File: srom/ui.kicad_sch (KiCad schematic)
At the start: 8 parts

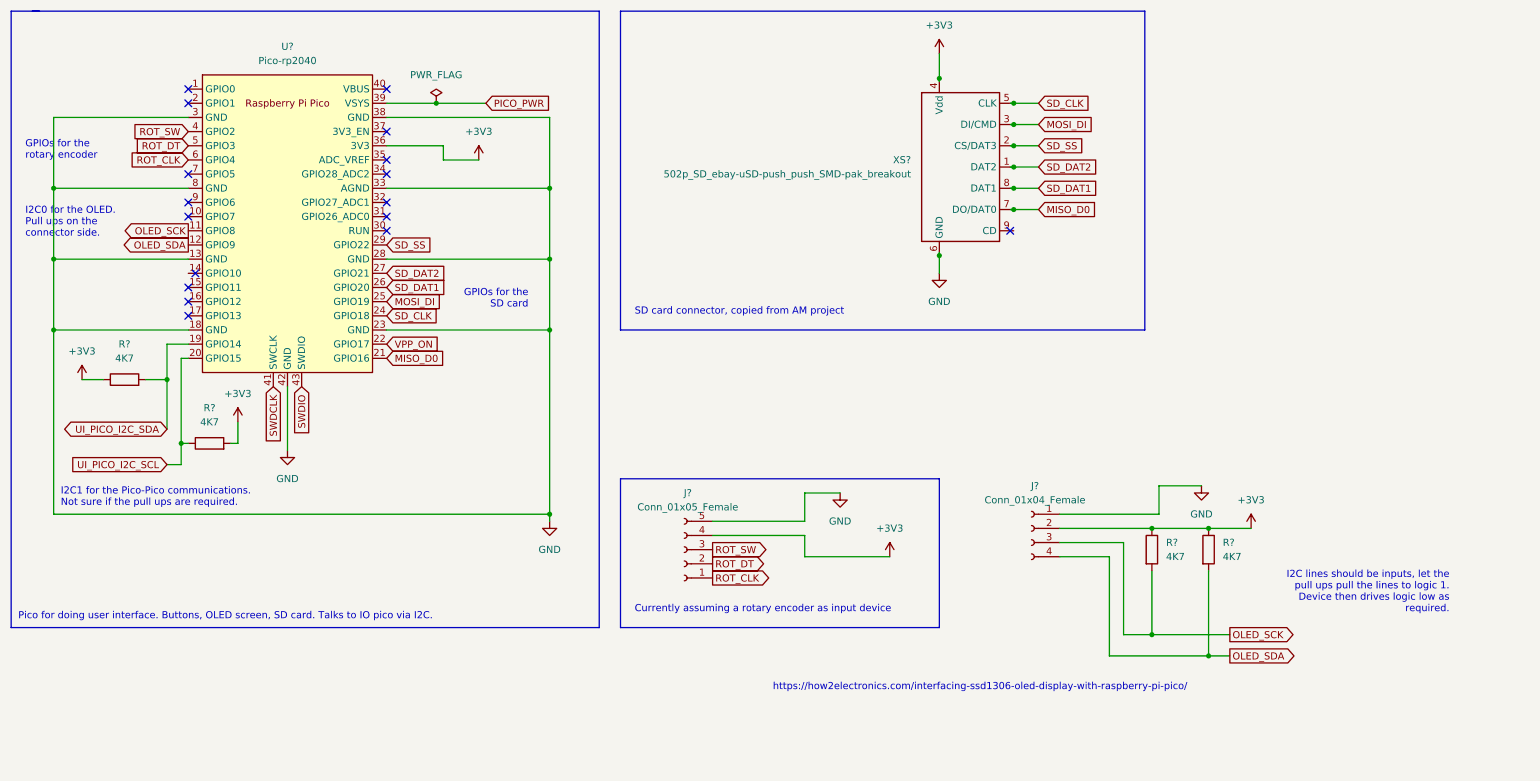
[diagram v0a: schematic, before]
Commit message: schematics complete for IO and UI picos
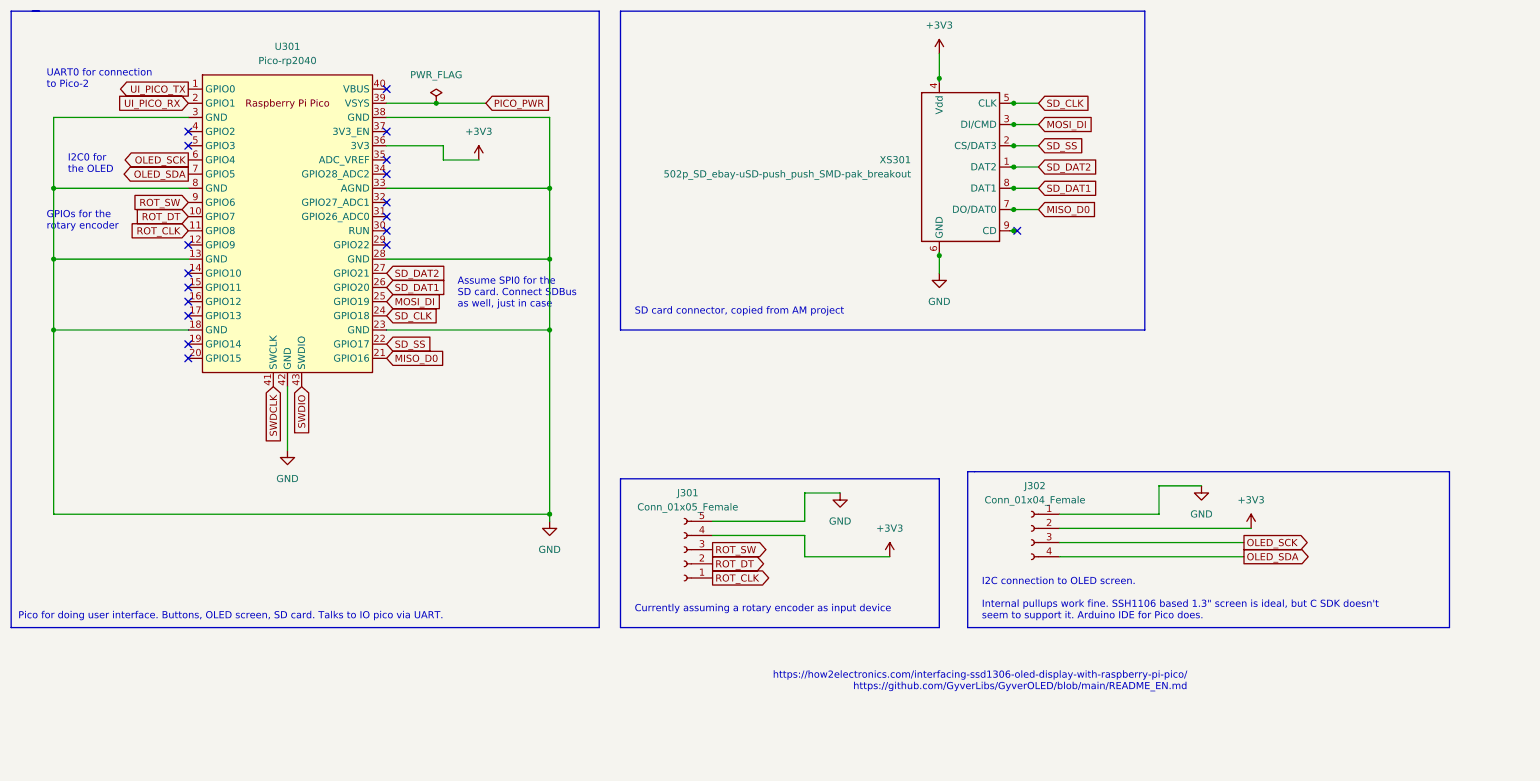
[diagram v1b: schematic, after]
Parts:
- removed R? (x4): 4K7, symbol Device:R
- gave numbers to parts that had none: 4
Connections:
- net VPP_ON is gone; now on net SD_SS: U301.22 (GPIO17)
- net OLED_SCK: now also U301.6 (GPIO4); no longer U301.11 (GPIO8)
- net OLED_SDA: now also U301.7 (GPIO5); no longer U301.12 (GPIO9)
- net ROT_CLK: now also U301.11 (GPIO8); no longer U301.6 (GPIO4)
- net ROT_DT: now also U301.10 (GPIO7); no longer U301.5 (GPIO3)
- net ROT_SW: now also U301.9 (GPIO6); no longer U301.4 (GPIO2)
- net SD_SS: no longer U301.29 (GPIO22)
- net UI_PICO_TX: now reaches U301.1 (GPIO0)
- net UI_PICO_RX: now reaches U301.2 (GPIO1)
- net UI_PICO_I2C_SCL: no longer names the net of U301.20 (GPIO15)
- net UI_PICO_I2C_SDA: no longer names the net of U301.19 (GPIO14)
- no-connect marks 17 -> 18
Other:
- note added: "Assume SPI0 for the SD card. Connect SDBus as well, just in case"
- note added: "I2C connection to OLED screen. Internal pullups work fine. SSH1106 based 1.3" screen is ideal, but C SDK doesn't seem to support it. Arduino IDE for Pico does."
- note added: "I2C0 for the OLED"
- note added: "Pico for doing user interface. Buttons, OLED screen, SD card. Talks to IO pico via UART."
- note added: "UART0 for connection to Pico-2"
- note added: "https://how2electronics.com/interfacing-ssd1306-oled-display-with-raspberry-pi-pico/ https://github.com/GyverLibs/GyverOLED/blob/main/README_EN.md"
- note removed: "GPIOs for the SD card"
- note removed: "I2C lines should be inputs, let the pull ups pull the lines to logic 1. Device then drives logic low as required."
- note removed: "I2C0 for the OLED. Pull ups on the connector side."
- note removed: "I2C1 for the Pico-Pico communications. Not sure if the pull ups are required."
- note removed: "Pico for doing user interface. Buttons, OLED screen, SD card. Talks to IO pico via I2C."
- note removed: "https://how2electronics.com/interfacing-ssd1306-oled-display-with-raspberry-pi-pico/"

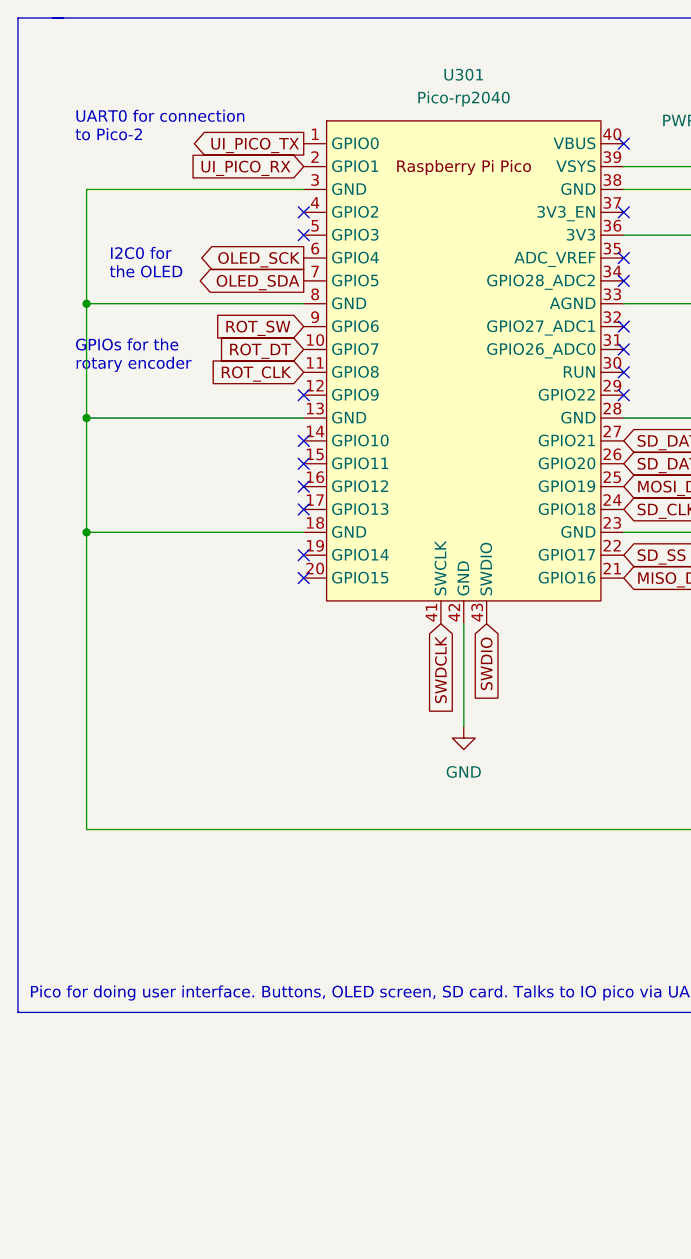
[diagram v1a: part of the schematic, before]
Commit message: first draft pcb layout
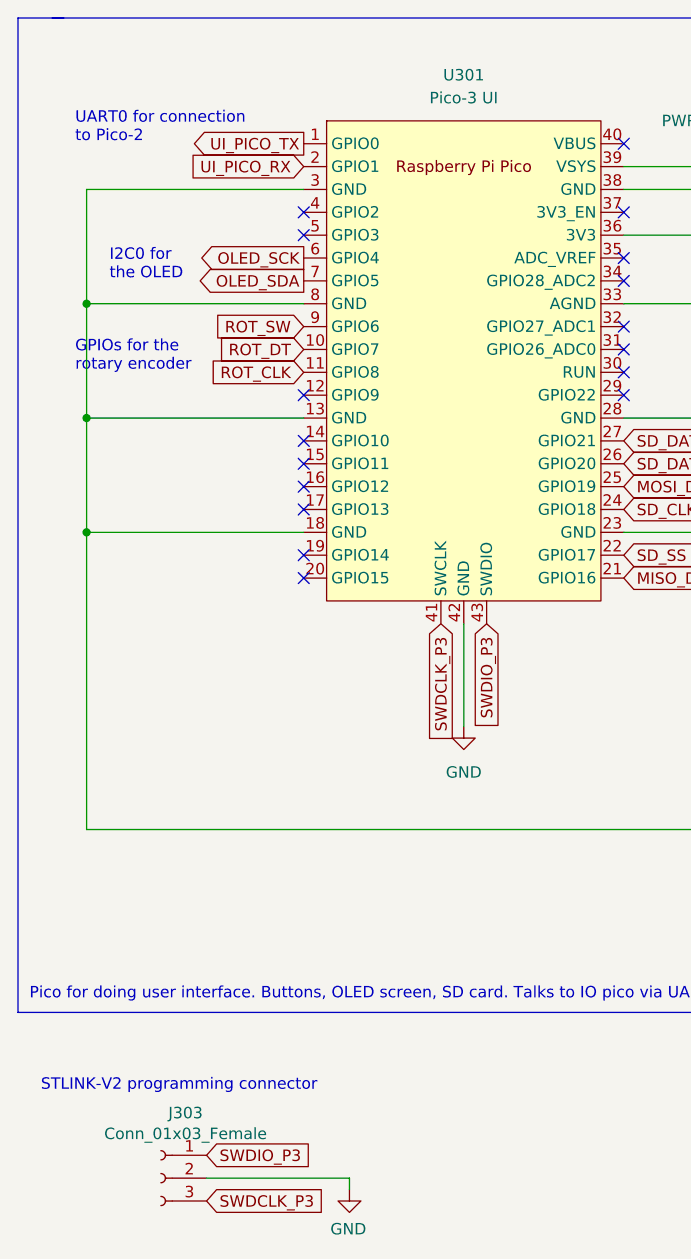
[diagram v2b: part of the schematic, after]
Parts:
- added J303: Conn_01x03_Female, Connector_PinHeader_2.54mm:PinHeader_1x03_P2.54mm_Vertical, symbol Connector:Conn_01x03_Female
- J301: footprint (none) -> Connector_PinHeader_2.54mm:PinHeader_1x05_P2.54mm_Vertical
- J302: footprint (none) -> Connector_PinHeader_2.54mm:PinHeader_1x04_P2.54mm_Vertical
- U301: value Pico-rp2040 -> Pico-3 UI
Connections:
- net GND: now also J303.2 (Pin_2)
- net SWDCLK renamed SWDCLK_P3
- net SWDCLK_P3: now also J303.3 (Pin_3)
- net SWDIO renamed SWDIO_P3
- net SWDIO_P3: now also J303.1 (Pin_1)
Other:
- note added: "STLINK-V2 programming connector"
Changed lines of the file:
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@@
+    (stroke (width 0) (type default) (color 0 0 0 0))
+  )
+  (wire (pts (xy 59.69 150.495) (xy 43.815 150.495))
     (stroke (width 0) (type default) (color 0 0 0 0))
   )
@@
   )
   (polyline (pts (xy 132.08 21.59) (xy 226.06 21.59))
+    (stroke (width 0) (type default) (color 0 0 0 0))
+  )
+  (wire (pts (xy 59.69 151.765) (xy 59.69 150.495))
     (stroke (width 0) (type default) (color 0 0 0 0))
   )
@@
   (text "Pico for doing user interface. Buttons, OLED screen, SD card. Talks to IO pico via UART."
     (at 24.13 130.81 0)
+    (effects (font (size 1.27 1.27)) (justify left bottom))
+  )
+  (text "STLINK-V2 programming connector" (at 25.4 140.97 0)
     (effects (font (size 1.27 1.27)) (justify left bottom))
   )
@@
     (effects (font (size 1.27 1.27)) (justify left bottom))
   )
-  (global_label "SWDCLK" (shape input) (at 69.85 88.9 270) (fields_autoplaced)
-    (effects (font (size 1.27 1.27)) (justify right))
-    (property "Intersheet References" "${INTERSHEET_REFS}" (id 0) (at 189.23 -68.58 0)
-      (effects (font (size 1.27 1.27)) hide)
-    )
-  )
-  (global_label "SWDIO" (shape input) (at 74.93 88.9 270) (fields_autoplaced)
-    (effects (font (size 1.27 1.27)) (justify right))
-    (property "Intersheet References" "${INTERSHEET_REFS}" (id 0) (at 189.23 -68.58 0)
-      (effects (font (size 1.27 1.27)) hide)
+  (global_label "SWDCLK_P3" (shape input) (at 69.85 88.9 270) (fields_autoplaced)
+    (effects (font (size 1.27 1.27)) (justify right))
+    (property "Intersheet References" "${INTERSHEET_REFS}" (id 0) (at 69.7706 102.2593 90)
+      (effects (font (size 1.27 1.27)) (justify right) hide)
+    )
+  )
+  (global_label "SWDIO_P3" (shape input) (at 74.93 88.9 270) (fields_autoplaced)
+    (effects (font (size 1.27 1.27)) (justify right))
+    (property "Intersheet References" "${INTERSHEET_REFS}" (id 0) (at 74.8506 100.6264 90)
+      (effects (font (size 1.27 1.27)) (justify right) hide)
     )
   )
@@
     )
   )
+  (global_label "SWDCLK_P3" (shape input) (at 43.815 153.035 0) (fields_autoplaced)
+    (effects (font (size 1.27 1.27)) (justify left))
+    (property "Intersheet References" "${INTERSHEET_REFS}" (id 0) (at 57.1743 152.9556 0)
+      (effects (font (size 1.27 1.27)) (justify left) hide)
+    )
+  )
   (global_label "ROT_SW" (shape output) (at 148.59 118.11 0) (fields_autoplaced)
     (effects (font (size 1.27 1.27)) (justify left))
@@
     (effects (font (size 1.27 1.27)) (justify left))
     (property "Intersheet References" "${INTERSHEET_REFS}" (id 0) (at 255.7479 116.7606 0)
+      (effects (font (size 1.27 1.27)) (justify left) hide)
+    )
+  )
+  (global_label "SWDIO_P3" (shape input) (at 43.815 147.955 0) (fields_autoplaced)
+    (effects (font (size 1.27 1.27)) (justify left))
+    (property "Intersheet References" "${INTERSHEET_REFS}" (id 0) (at 55.5414 147.8756 0)
       (effects (font (size 1.27 1.27)) (justify left) hide)
     )
@@
     )
     (property "Datasheet" "~" (id 3) (at 99.06 38.1 0)
+      (effects (font (size 1.27 1.27)) hide)
+    )
+    (pin "1")
+  )
+  (symbol (lib_id "power:GND") (at 59.69 151.765 0) (mirror y) (unit 1)
+    (in_bom yes) (on_board yes)
+    (property "Reference" "#PWR0310" (id 0) (at 59.69 158.115 0)
+      (effects (font (size 1.27 1.27)) hide)
+    )
+    (property "Value" "GND" (id 1) (at 59.563 156.1592 0))
+    (property "Footprint" "" (id 2) (at 59.69 151.765 0)
+      (effects (font (size 1.27 1.27)) hide)
+    )
+    (property "Datasheet" "" (id 3) (at 59.69 151.765 0)
       (effects (font (size 1.27 1.27)) hide)
     )
@@
     (pin "1")
   )
+  (symbol (lib_id "Connector:Conn_01x03_Female") (at 38.735 150.495 0) (mirror y) (unit 1)
+    (in_bom yes) (on_board yes)
+    (property "Reference" "J303" (id 0) (at 41.4782 143.256 0))
+    (property "Value" "Conn_01x03_Female" (id 1) (at 41.4782 145.5674 0))
+    (property "Footprint" "Connector_PinHeader_2.54mm:PinHeader_1x03_P2.54mm_Vertical" (id 2) (at 38.735 150.495 0)
+      (effects (font (size 1.27 1.27)) hide)
+    )
+    (property "Datasheet" "~" (id 3) (at 38.735 150.495 0)
+      (effects (font (size 1.27 1.27)) hide)
+    )
+    (pin "1")
+    (pin "2")
+    (pin "3")
+  )
   (symbol (lib_id "power:+3V3") (at 189.23 29.21 0) (unit 1)
     (in_bom yes) (on_board yes) (fields_autoplaced)
@@
     (in_bom yes) (on_board yes) (fields_autoplaced)
     (property "Reference" "U301" (id 0) (at 72.39 27.94 0))
-    (property "Value" "Pico-rp2040" (id 1) (at 72.39 30.48 0))
+    (property "Value" "Pico-3 UI" (id 1) (at 72.39 30.48 0))
     (property "Footprint" "pico-foot:RPi_Pico_SMD_TH" (id 2) (at 72.39 59.69 90)
       (effects (font (size 1.27 1.27)) hide)
@@
     (property "Reference" "J302" (id 0) (at 206.375 106.68 0))
     (property "Value" "Conn_01x04_Female" (id 1) (at 206.375 109.22 0))
-    (property "Footprint" "" (id 2) (at 205.74 114.3 0)
+    (property "Footprint" "Connector_PinHeader_2.54mm:PinHeader_1x04_P2.54mm_Vertical" (id 2) (at 205.74 114.3 0)
       (effects (font (size 1.27 1.27)) hide)
     )
@@
     (property "Reference" "J301" (id 0) (at 144.145 107.95 0))
     (property "Value" "Conn_01x05_Female" (id 1) (at 144.145 110.49 0))
-    (property "Footprint" "" (id 2) (at 143.51 118.11 0)
-      (effects (font (size 1.27 1.27)) hide)
-    )
+    (property "Footprint" "Connector_PinHeader_2.54mm:PinHeader_1x05_P2.54mm_Vertical" (id 2) (at 143.51 118.11 0)
+      (effects (font (size 1.27 1.27)) hide)
+    )

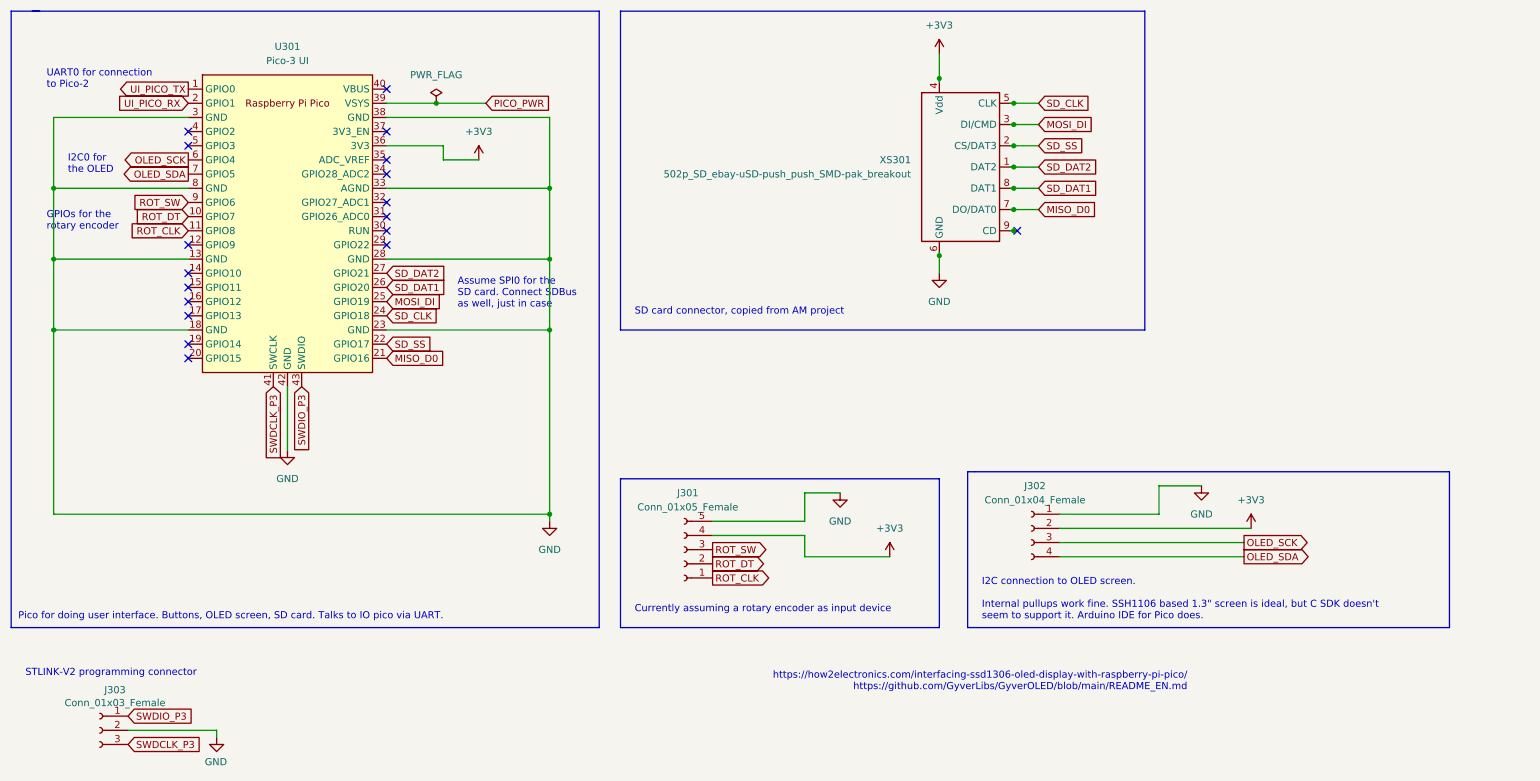
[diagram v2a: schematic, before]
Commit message: break out the 3V3 supplies into separate ones
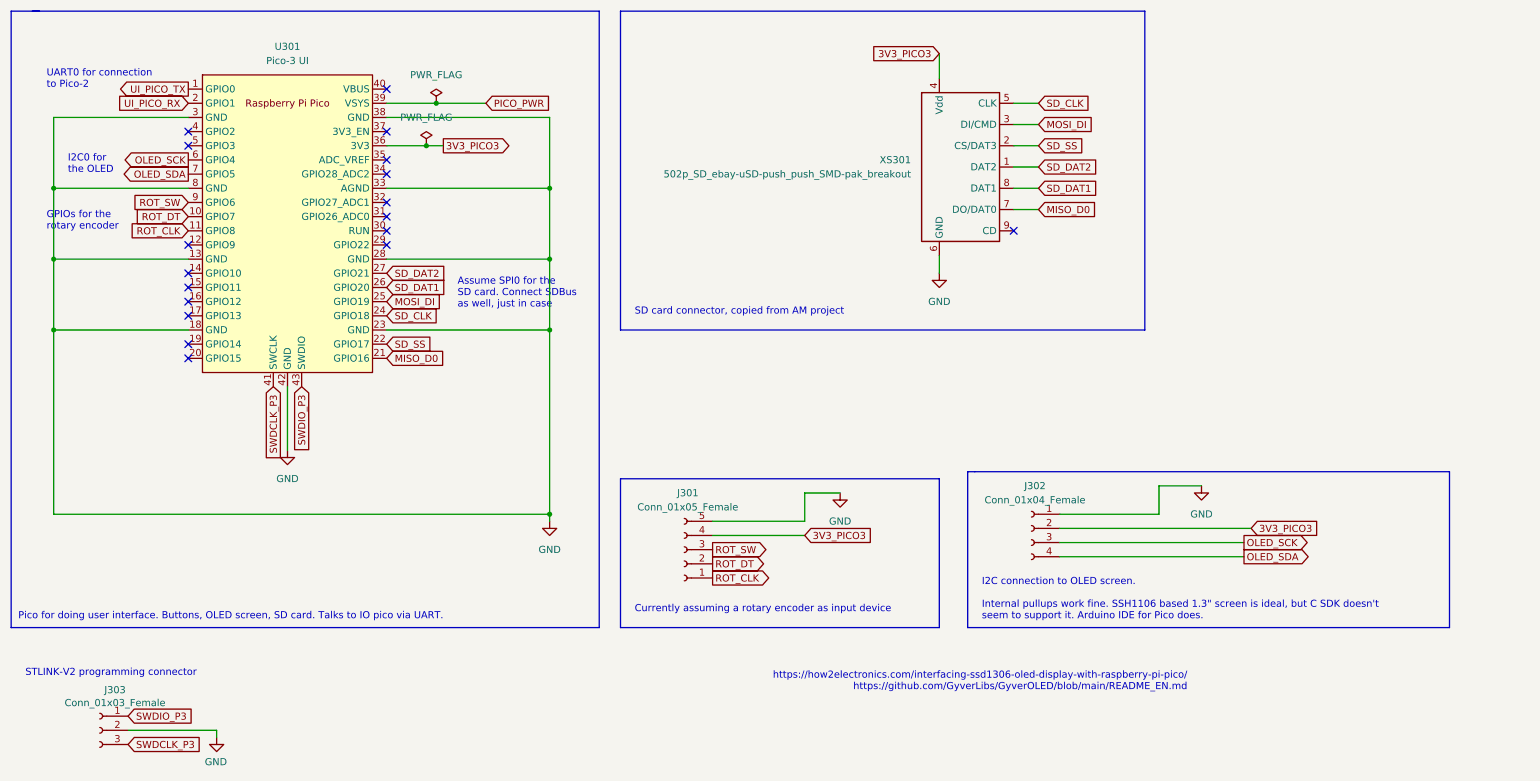
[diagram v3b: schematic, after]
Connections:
- net +3V3 renamed 3V3_PICO3
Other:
- title: (none) -> Pico Interface One
